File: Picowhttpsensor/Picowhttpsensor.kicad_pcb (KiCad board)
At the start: 2 copper layers, 2 parts, among them J1 Z-ICS0S40P-W000, U1 Pico

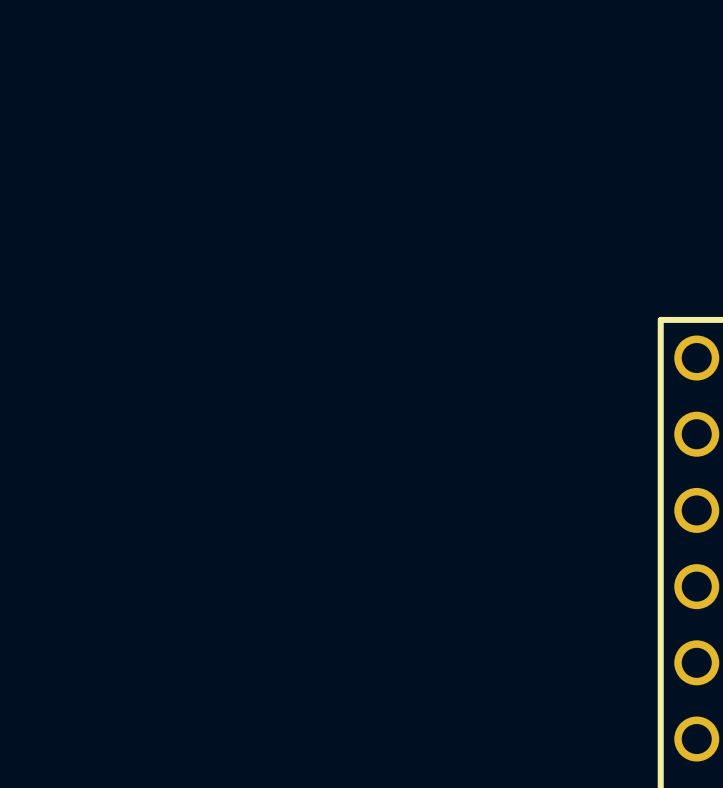
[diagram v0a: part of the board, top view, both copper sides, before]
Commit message: add aht20
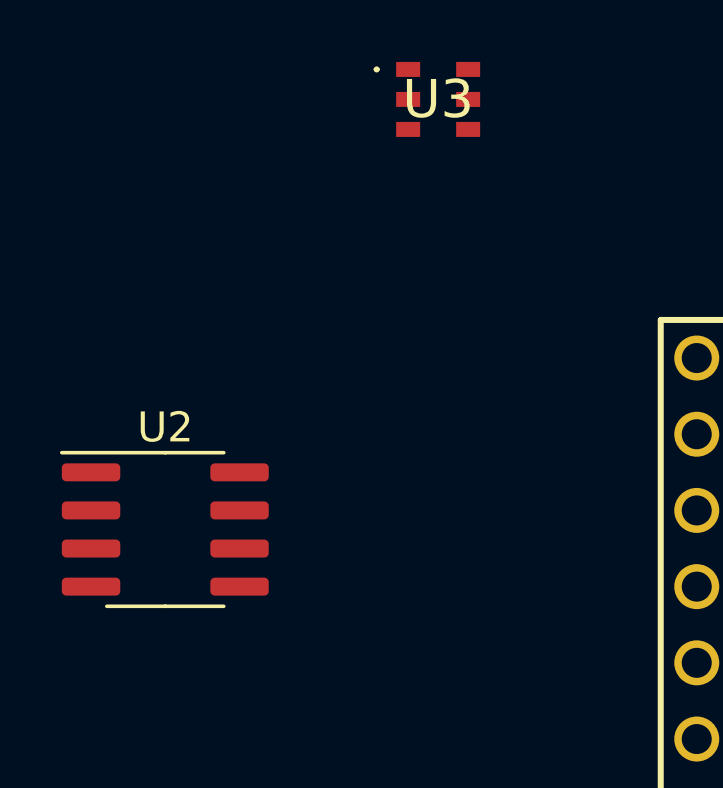
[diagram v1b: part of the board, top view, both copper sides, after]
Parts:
- added U2: PCF8523T, Package_SO:SOIC-8_3.9x4.9mm_P1.27mm, F.Cu at (55.9, 69.2)
- added U3: AHT20, AHT20:AHT20, F.Cu at (65.0, 54.9)
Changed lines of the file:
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@@
   (net 82 "unconnected-(J1-Pad39)")
   (net 83 "unconnected-(J1-Pad40)")
+  (net 84 "unconnected-(U2-OSCI-Pad1)")
+  (net 85 "unconnected-(U2-OSCO-Pad2)")
+  (net 86 "unconnected-(U2-VBAT-Pad3)")
+  (net 87 "unconnected-(U2-VSS-Pad4)")
+  (net 88 "unconnected-(U2-SDA-Pad5)")
+  (net 89 "unconnected-(U2-SCL-Pad6)")
+  (net 90 "unconnected-(U2-~{INT1}{slash}CLKOUT-Pad7)")
+  (net 91 "unconnected-(U2-VDD-Pad8)")
+  (net 92 "unconnected-(U3-NC_1-Pad1)")
+  (net 93 "unconnected-(U3-VDD-Pad2)")
+  (net 94 "unconnected-(U3-SCL-Pad3)")
+  (net 95 "unconnected-(U3-SDA-Pad4)")
+  (net 96 "unconnected-(U3-GND-Pad5)")
+  (net 97 "unconnected-(U3-NC_2-Pad6)")
   (footprint "Z-ICS0S40P-W000:ZICS0S40PW000" (layer "F.Cu")
     (at 88.9 111.76 90)
@@
       (net 43 "unconnected-(U1-SWDIO-Pad43)") (pinfunction "SWDIO") (pintype "bidirectional"))
   )
+  (footprint "AHT20:AHT20" (layer "F.Cu")
+    (at 65.04 54.88)
+    (descr "AHT20-1")
+    (tags "Undefined or Miscellaneous")
+    (property "Arrow Part Number" "")
+    (property "Arrow Price/Stock" "")
+    (property "Description" "Integrated temperature and humidity Sensor DC : 2.2 - 5.5V, 0 ~{} 100% RH, -40 ~{} + 85 .")
+    (property "Height" "1.1")
+    (property "Manufacturer_Name" "Aosong")
+    (property "Manufacturer_Part_Number" "AHT20")
+    (property "Mouser Part Number" "")
+    (property "Mouser Price/Stock" "")
+    (property "Sheetfile" "Picowhttpsensor.kicad_sch")
+    (property "Sheetname" "")
+    (property "ki_description" "Integrated temperature and humidity Sensor DC : 2.2 - 5.5V, 0 ~ 100% RH, -40 ~ + 85 .")
+    (attr smd)
+    (fp_text reference "U3" (at 0 0) (layer "F.SilkS")
+        (effects (font (size 1.27 1.27) (thickness 0.254)))
+    )
+    (fp_text value "AHT20" (at 0 0) (layer "F.SilkS") hide
+        (effects (font (size 1.27 1.27) (thickness 0.254)))
+    )
+    (fp_text user "${REFERENCE}" (at 0 0) (layer "F.Fab")
+        (effects (font (size 1.27 1.27) (thickness 0.254)))
+    )
+    (fp_line (start -2.1 -1) (end -2.1 -1)
+      (stroke (width 0.1) (type solid)) (layer "F.SilkS"))
+    (fp_line (start -2 -1) (end -2 -1)
+      (stroke (width 0.1) (type solid)) (layer "F.SilkS"))
+    (fp_arc (start -2.1 -1) (mid -2.05 -1.05) (end -2 -1)
+      (stroke (width 0.1) (type solid)) (layer "F.SilkS"))
+    (fp_arc (start -2 -1) (mid -2.05 -0.95) (end -2.1 -1)
+      (stroke (width 0.1) (type solid)) (layer "F.SilkS"))
+    (fp_line (start -2.5 -2.5) (end 2.5 -2.5)
+      (stroke (width 0.1) (type solid)) (layer "F.CrtYd"))
+    (fp_line (start -2.5 2.5) (end -2.5 -2.5)
+      (stroke (width 0.1) (type solid)) (layer "F.CrtYd"))
+    (fp_line (start 2.5 -2.5) (end 2.5 2.5)
+      (stroke (width 0.1) (type solid)) (layer "F.CrtYd"))
+    (fp_line (start 2.5 2.5) (end -2.5 2.5)
+      (stroke (width 0.1) (type solid)) (layer "F.CrtYd"))
+    (fp_line (start -1.5 -1.5) (end 1.5 -1.5)
+      (stroke (width 0.1) (type solid)) (layer "F.Fab"))
+    (fp_line (start -1.5 1.5) (end -1.5 -1.5)
+      (stroke (width 0.1) (type solid)) (layer "F.Fab"))
+    (fp_line (start 1.5 -1.5) (end 1.5 1.5)
+      (stroke (width 0.1) (type solid)) (layer "F.Fab"))
+    (fp_line (start 1.5 1.5) (end -1.5 1.5)
+      (stroke (width 0.1) (type solid)) (layer "F.Fab"))
+    (pad "1" smd rect (at -1 -1 90) (size 0.5 0.8) (layers "F.Cu" "F.Paste" "F.Mask")
+      (net 92 "unconnected-(U3-NC_1-Pad1)") (pinfunction "NC_1") (pintype "passive"))
+    (pad "2" smd rect (at -1 0 90) (size 0.5 0.8) (layers "F.Cu" "F.Paste" "F.Mask")
+      (net 93 "unconnected-(U3-VDD-Pad2)") (pinfunction "VDD") (pintype "passive"))
+    (pad "3" smd rect (at -1 1 90) (size 0.5 0.8) (layers "F.Cu" "F.Paste" "F.Mask")
+      (net 94 "unconnected-(U3-SCL-Pad3)") (pinfunction "SCL") (pintype "passive"))
+    (pad "4" smd rect (at 1 1 90) (size 0.5 0.8) (layers "F.Cu" "F.Paste" "F.Mask")
+      (net 95 "unconnected-(U3-SDA-Pad4)") (pinfunction "SDA") (pintype "passive"))
+    (pad "5" smd rect (at 1 0 90) (size 0.5 0.8) (layers "F.Cu" "F.Paste" "F.Mask")
+      (net 96 "unconnected-(U3-GND-Pad5)") (pinfunction "GND") (pintype "passive"))
+    (pad "6" smd rect (at 1 -1 90) (size 0.5 0.8) (layers "F.Cu" "F.Paste" "F.Mask")
+      (net 97 "unconnected-(U3-NC_2-Pad6)") (pinfunction "NC_2") (pintype "passive"))
+    (model "AHT20.stp"
+      (offset (xyz 0 0 0))
+      (scale (xyz 1 1 1))
+      (rotate (xyz 0 0 0))
+    )
+  )
+  (footprint "Package_SO:SOIC-8_3.9x4.9mm_P1.27mm" (layer "F.Cu")
+    (at 55.945 69.215)
+    (descr "SOIC, 8 Pin (JEDEC MS-012AA, https://www.analog.com/media/en/package-pcb-resources/package/pkg_pdf/soic_narrow-r/r_8.pdf), generated with kicad-footprint-generator ipc_gullwing_generator.py")
+    (tags "SOIC SO")
+    (property "Sheetfile" "Picowhttpsensor.kicad_sch")
+    (property "Sheetname" "")
+    (property "ki_description" "Realtime Clock/Calendar I2C Interface, SOIC-8")
+    (property "ki_keywords" "I2C RTC Clock Calendar")
+    (attr smd)
+    (fp_text reference "U2" (at 0 -3.4) (layer "F.SilkS")
+        (effects (font (size 1 1) (thickness 0.15)))
+    )
+    (fp_text value "PCF8523T" (at 0 3.4) (layer "F.Fab")
+        (effects (font (size 1 1) (thickness 0.15)))
+    )
+    (fp_text user "${REFERENCE}" (at 0 0) (layer "F.Fab")
+        (effects (font (size 0.98 0.98) (thickness 0.15)))
+    )
+    (fp_line (start 0 -2.56) (end -3.45 -2.56)
+      (stroke (width 0.12) (type solid)) (layer "F.SilkS"))
+    (fp_line (start 0 -2.56) (end 1.95 -2.56)
+      (stroke (width 0.12) (type solid)) (layer "F.SilkS"))
+    (fp_line (start 0 2.56) (end -1.95 2.56)
+      (stroke (width 0.12) (type solid)) (layer "F.SilkS"))
+    (fp_line (start 0 2.56) (end 1.95 2.56)
+      (stroke (width 0.12) (type solid)) (layer "F.SilkS"))
+    (fp_line (start -3.7 -2.7) (end -3.7 2.7)
+      (stroke (width 0.05) (type solid)) (layer "F.CrtYd"))
+    (fp_line (start -3.7 2.7) (end 3.7 2.7)
+      (stroke (width 0.05) (type solid)) (layer "F.CrtYd"))
+    (fp_line (start 3.7 -2.7) (end -3.7 -2.7)
+      (stroke (width 0.05) (type solid)) (layer "F.CrtYd"))
+    (fp_line (start 3.7 2.7) (end 3.7 -2.7)
+      (stroke (width 0.05) (type solid)) (layer "F.CrtYd"))
+    (fp_line (start -1.95 -1.475) (end -0.975 -2.45)
+      (stroke (width 0.1) (type solid)) (layer "F.Fab"))
+    (fp_line (start -1.95 2.45) (end -1.95 -1.475)
+      (stroke (width 0.1) (type solid)) (layer "F.Fab"))
+    (fp_line (start -0.975 -2.45) (end 1.95 -2.45)
+      (stroke (width 0.1) (type solid)) (layer "F.Fab"))
+    (fp_line (start 1.95 -2.45) (end 1.95 2.45)
+      (stroke (width 0.1) (type solid)) (layer "F.Fab"))
+    (fp_line (start 1.95 2.45) (end -1.95 2.45)
+      (stroke (width 0.1) (type solid)) (layer "F.Fab"))
+    (pad "1" smd roundrect (at -2.475 -1.905) (size 1.95 0.6) (layers "F.Cu" "F.Paste" "F.Mask") (roundrect_rratio 0.25)
+      (net 84 "unconnected-(U2-OSCI-Pad1)") (pinfunction "OSCI") (pintype "input"))
+    (pad "2" smd roundrect (at -2.475 -0.635) (size 1.95 0.6) (layers "F.Cu" "F.Paste" "F.Mask") (roundrect_rratio 0.25)
+      (net 85 "unconnected-(U2-OSCO-Pad2)") (pinfunction "OSCO") (pintype "output"))
+    (pad "3" smd roundrect (at -2.475 0.635) (size 1.95 0.6) (layers "F.Cu" "F.Paste" "F.Mask") (roundrect_rratio 0.25)
+      (net 86 "unconnected-(U2-VBAT-Pad3)") (pinfunction "VBAT") (pintype "power_in"))
+    (pad "4" smd roundrect (at -2.475 1.905) (size 1.95 0.6) (layers "F.Cu" "F.Paste" "F.Mask") (roundrect_rratio 0.25)
+      (net 87 "unconnected-(U2-VSS-Pad4)") (pinfunction "VSS") (pintype "power_in"))
+    (pad "5" smd roundrect (at 2.475 1.905) (size 1.95 0.6) (layers "F.Cu" "F.Paste" "F.Mask") (roundrect_rratio 0.25)
+      (net 88 "unconnected-(U2-SDA-Pad5)") (pinfunction "SDA") (pintype "bidirectional"))
+    (pad "6" smd roundrect (at 2.475 0.635) (size 1.95 0.6) (layers "F.Cu" "F.Paste" "F.Mask") (roundrect_rratio 0.25)
+      (net 89 "unconnected-(U2-SCL-Pad6)") (pinfunction "SCL") (pintype "input"))
+    (pad "7" smd roundrect (at 2.475 -0.635) (size 1.95 0.6) (layers "F.Cu" "F.Paste" "F.Mask") (roundrect_rratio 0.25)
+      (net 90 "unconnected-(U2-~{INT1}{slash}CLKOUT-Pad7)") (pinfunction "~{INT1}/CLKOUT") (pintype "open_collector"))
+    (pad "8" smd roundrect (at 2.475 -1.905) (size 1.95 0.6) (layers "F.Cu" "F.Paste" "F.Mask") (roundrect_rratio 0.25)
+      (net 91 "unconnected-(U2-VDD-Pad8)") (pinfunction "VDD") (pintype "power_in"))
+    (model "${KICAD6_3DMODEL_DIR}/Package_SO.3dshapes/SOIC-8_3.9x4.9mm_P1.27mm.wrl"
+      (offset (xyz 0 0 0))
+      (scale (xyz 1 1 1))
+      (rotate (xyz 0 0 0))
+    )
+  )
 )
